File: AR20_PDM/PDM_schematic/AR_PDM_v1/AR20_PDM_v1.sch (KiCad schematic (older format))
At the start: 21 parts, among them J1 S_T_?, J2 1-776163-1, U1 ACM_2020

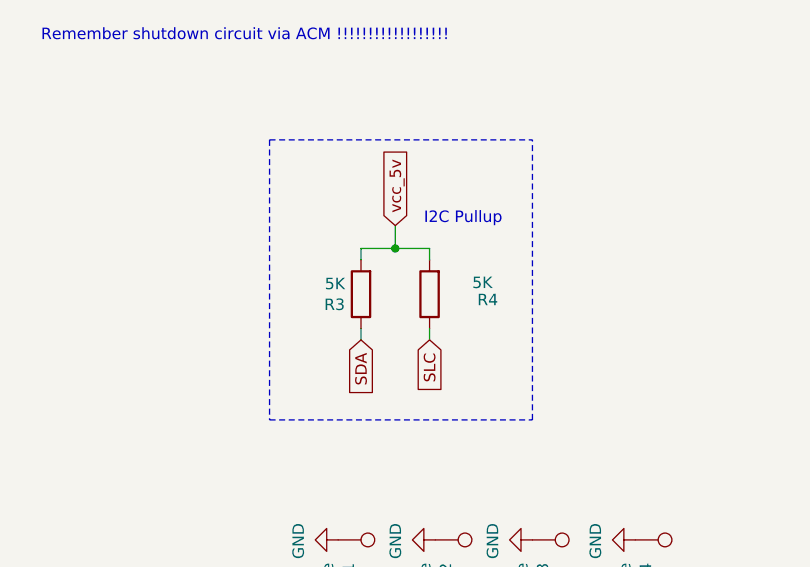
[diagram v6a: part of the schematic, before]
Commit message: Calculated and changes i2c pullup Resistors to 2 K
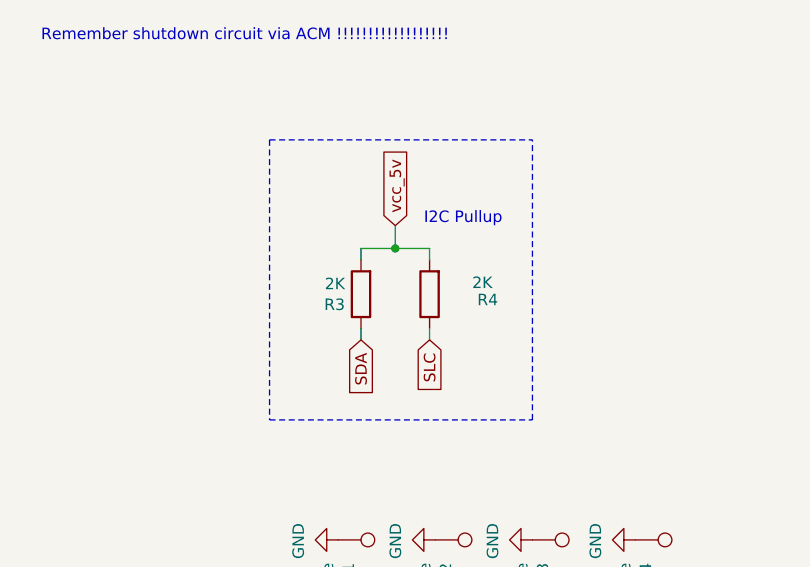
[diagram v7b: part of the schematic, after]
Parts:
- R3, R4: value 5K -> 2K
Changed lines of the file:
@@
 AR Path="/5DAD3BC1" Ref="R3"  Part="1"
 F 0 "R3" H 13545 4671 50  0000 L CNN
-F 1 "5K" H 13545 4580 50  0000 L CNN
+F 1 "2K" H 13545 4580 50  0000 L CNN
 F 2 "Resistor_SMD:R_0603_1608Metric" V 13405 4625 50  0001 C CNN
 F 3 "~" H 13475 4625 50  0001 C CNN
@@
 AR Path="/5E228553" Ref="R4"  Part="1"
 F 0 "R4" H 13475 4650 50  0000 L CNN
-F 1 "5K" H 13500 4575 50  0000 L CNN
+F 1 "2K" H 13500 4575 50  0000 L CNN
 F 2 "Resistor_SMD:R_0603_1608Metric" V 13705 4625 50  0001 C CNN
 F 3 "~" H 13775 4625 50  0001 C CNN

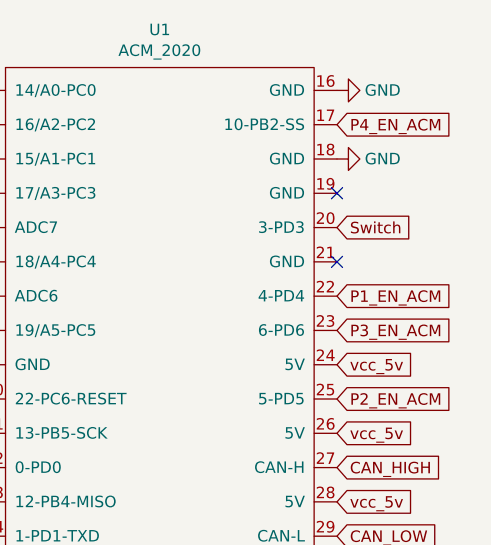
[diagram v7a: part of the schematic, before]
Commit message: Small tweaks, complete 3d render in ki-cad
- change switch pin with phase 1 enable, on the mcu, to get phase 1 PWM
switch can now be sampled with change interrupt.
- couple of traces beautified
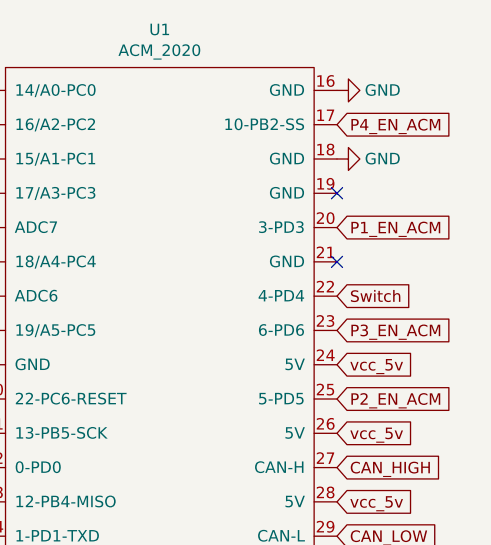
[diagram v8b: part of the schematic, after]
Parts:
- J1: footprint AR_PDM_v1:Wurth 74655095R Screw Post -> AR_PDM_v1:Wurth_74655095R_Screw_Post
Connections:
- net P1_EN_ACM: now also U1.20 (3-PD3); no longer U1.22 (4-PD4)
- net Switch: now also U1.22 (4-PD4); no longer U1.20 (3-PD3)
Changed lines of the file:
@@
 COIL_INJECTOR_Alert
 NoConn ~ 13625 1725
+Text GLabel 15175 1725 2    50   Input ~ 0
+Switch
 Text GLabel 15175 1425 2    50   Input ~ 0
-Switch
-Text GLabel 15175 1725 2    50   Input ~ 0
 P1_EN_ACM
 Text GLabel 2925 7075 0    50   Input ~ 0
@@
 F 0 "J1" V 1672 7605 50  0000 L CNN
 F 1 "S_T_?" V 1763 7605 50  0000 L CNN
-F 2 "AR_PDM_v1:Wurth 74655095R Screw Post" H 1800 7525 50  0001 C CNN
+F 2 "AR_PDM_v1:Wurth_74655095R_Screw_Post" H 1800 7525 50  0001 C CNN
 F 3 "~" H 1800 7525 50  0001 C CNN
 	1    1800 7525
